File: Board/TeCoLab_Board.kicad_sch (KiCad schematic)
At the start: 56 parts, among them J1 Jack, J2 Supply_Terminal, J3 DC Cooler, Q1 BC337, Q2 TIP122, Q3 TIP122, U1 DS18B20, U2 PC817, U3 DS18B20, U4 DS18B20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

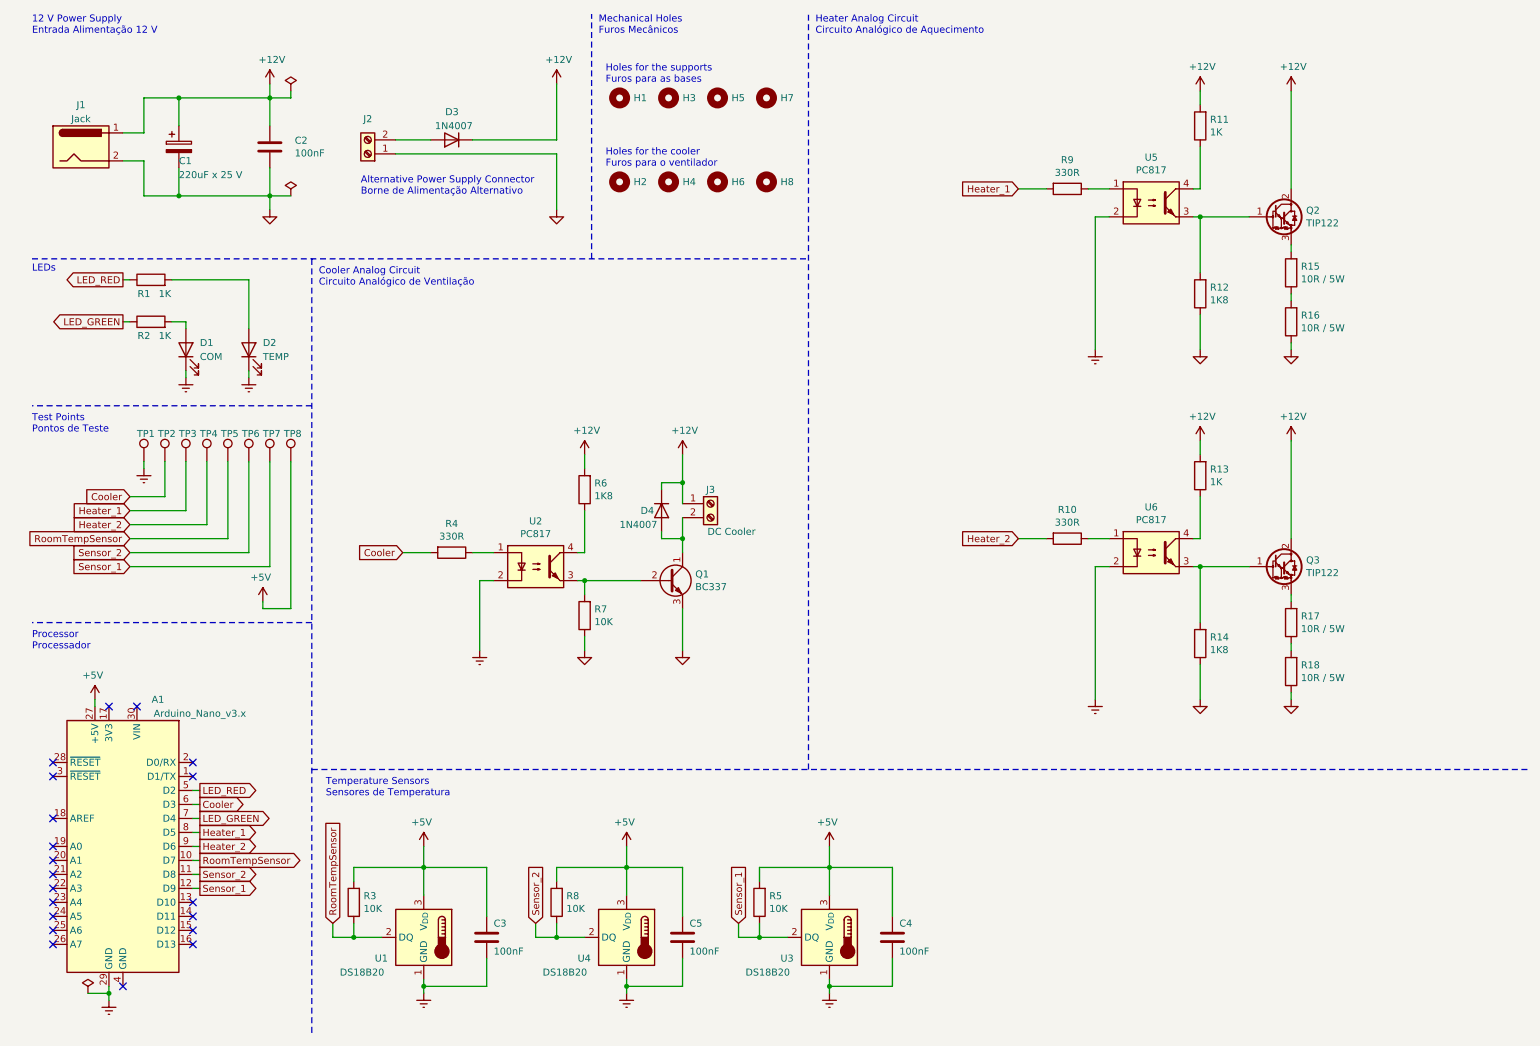
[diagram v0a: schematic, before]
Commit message: Update for KiCad 9.0 compatibility; remove gerbers from repository; Schematic: replaced 10K resistors by 4.7K resistors; PCB: replaced TO-92 package by its hand-soldering version.
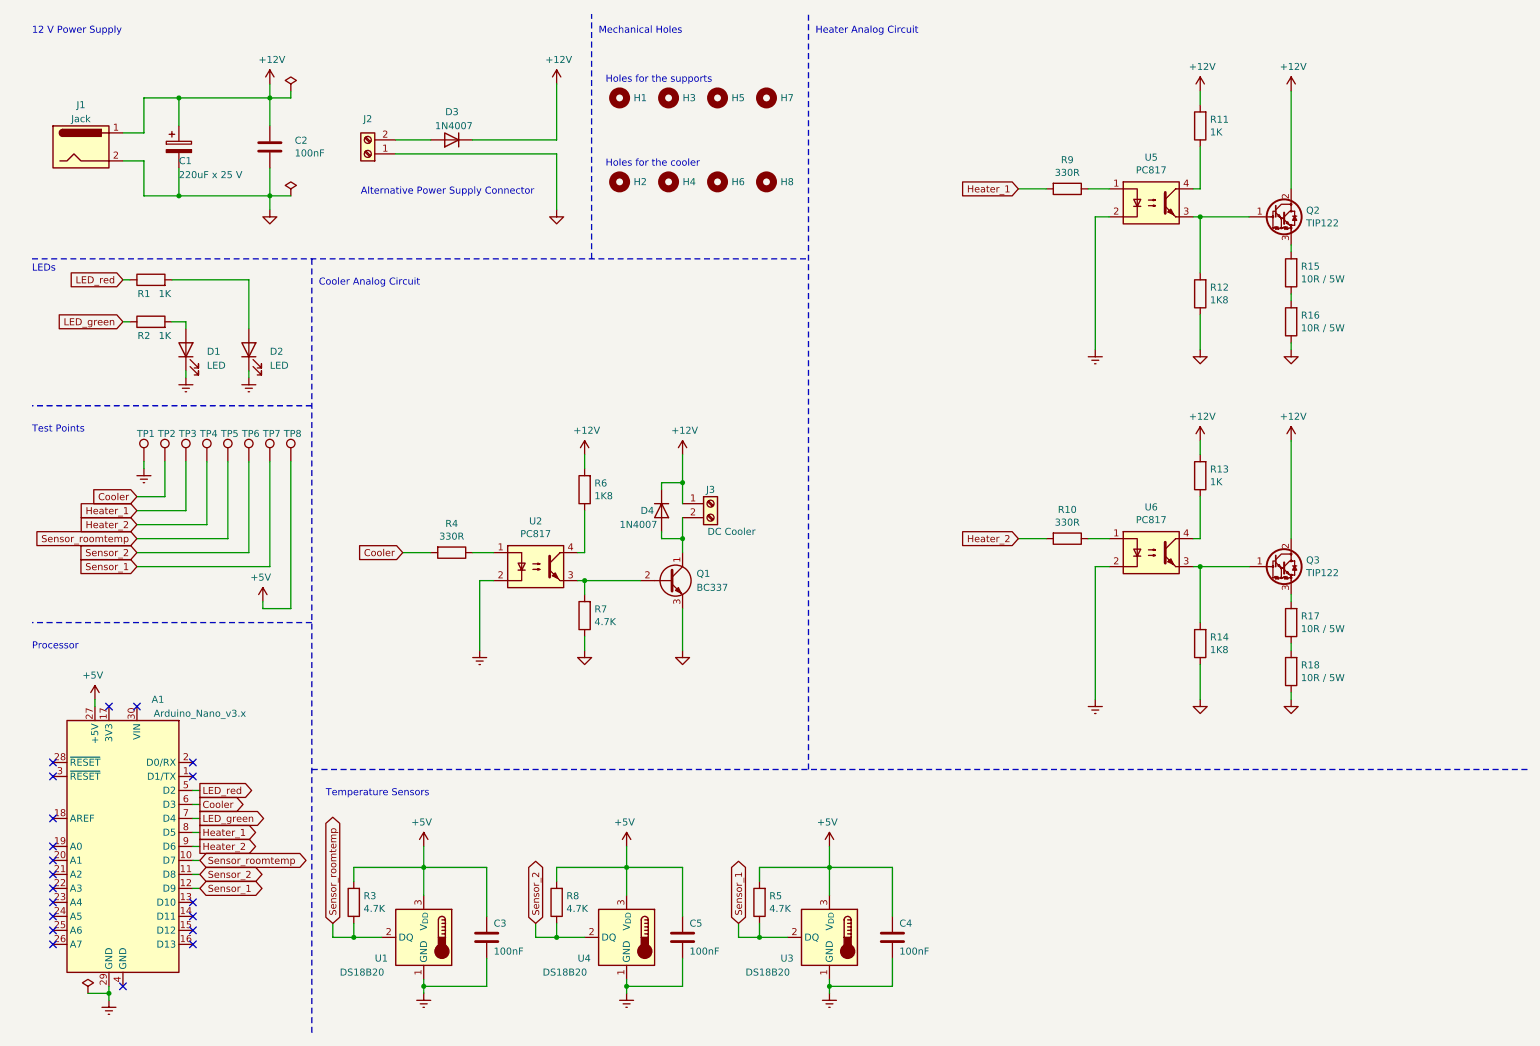
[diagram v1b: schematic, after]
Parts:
- D1: value COM -> LED
- D2: value TEMP -> LED
- Q1, U1, U3, U4: footprint Package_TO_SOT_THT:TO-92_Inline -> Package_TO_SOT_THT:TO-92_HandSolder
- R3, R5, R7, R8: value 10K -> 4.7K
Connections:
- net LED_GREEN renamed LED_green
- net LED_RED renamed LED_red
- net RoomTempSensor renamed Sensor_roomtemp
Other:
- note added: "12 V Power Supply"
- note added: "Alternative Power Supply Connector"
- note added: "Cooler Analog Circuit"
- note added: "Heater Analog Circuit"
- note added: "Holes for the cooler"
- note added: "Holes for the supports"
- note added: "Mechanical Holes"
- note added: "Processor"
- note added: "Temperature Sensors"
- note added: "Test Points"
- note removed: "12 V Power Supply Entrada Alimentação 12 V"
- note removed: "Alternative Power Supply Connector Borne de Alimentação Alternativo"
- note removed: "Cooler Analog Circuit Circuito Analógico de Ventilação"
- note removed: "Heater Analog Circuit Circuito Analógico de Aquecimento"
- note removed: "Holes for the cooler Furos para o ventilador"
- note removed: "Holes for the supports Furos para as bases"
- note removed: "Mechanical Holes Furos Mecânicos"
- note removed: "Processor Processador"
- note removed: "Temperature Sensors Sensores de Temperatura"
- note removed: "Test Points Pontos de Teste"
